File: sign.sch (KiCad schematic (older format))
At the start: 142 parts, among them J1 CONN_01X02, J2 CONN_01X02, J3 CONN_01X02, U1 APA102C_x6, U10 APA102C_x2, U100 APA102C_x6, U101 APA102C_x4, U102 APA102C_x2, U103 APA102C_x1, U104 APA102C_x3, U105 APA102C_x5, U106 APA102C_x2, U107 APA102C_x3, U108 APA102C_x10, U109 APA102C_x9, U11 APA102C_x2, U110 APA102C_x3, U111 APA102C_x12, U112 APA102C_x16, U113 APA102C_x8, U114 APA102C_x13, U115 APA102C_x3, U116 APA102C_x6, U117 APA102C_x3, U118 APA102C_x6, U119 APA102C_x3, U12 APA102C_x2, U120 APA102C_x2, U121 APA102C_x6, U122 APA102C_x3, U123 APA102C_x6, U124 APA102C_x7, U125 APA102C_x12, U126 APA102C_x6, U127 APA102C_x11, U128 APA102C_x4, U129 APA102C_x6, U13 APA102C_x2, U130 APA102C_x2, U131 APA102C_x2, U132 APA102C_x3, U133 APA102C_x1, U134 APA102C_x3, U135 APA102C_x3, U136 APA102C_x12, U137 APA102C_x12, U138 APA102C_x9, U139 APA102C_x4, U14 APA102C_x3, U15 APA102C_x3, U16 APA102C_x3, U17 APA102C_x3, U18 APA102C_x5, U19 APA102C_x6, U2 APA102C_x8, U20 APA102C_x2, U21 APA102C_x7, U22 APA102C_x5, U23 APA102C_x7, U24 APA102C_x3, U25 APA102C_x2, U26 APA102C_x7, U27 APA102C_x2, U28 APA102C_x3, U29 APA102C_x5, U3 APA102C_x11, U30 APA102C_x2, U31 APA102C_x5, U32 APA102C_x2, U33 APA102C_x8, U34 APA102C_x9, U35 APA102C_x3, U36 APA102C_x2, U37 APA102C_x5, U38 APA102C_x11, U39 APA102C_x6, U4 APA102C_x6, U40 APA102C_x4, U41 APA102C_x5, U42 APA102C_x3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

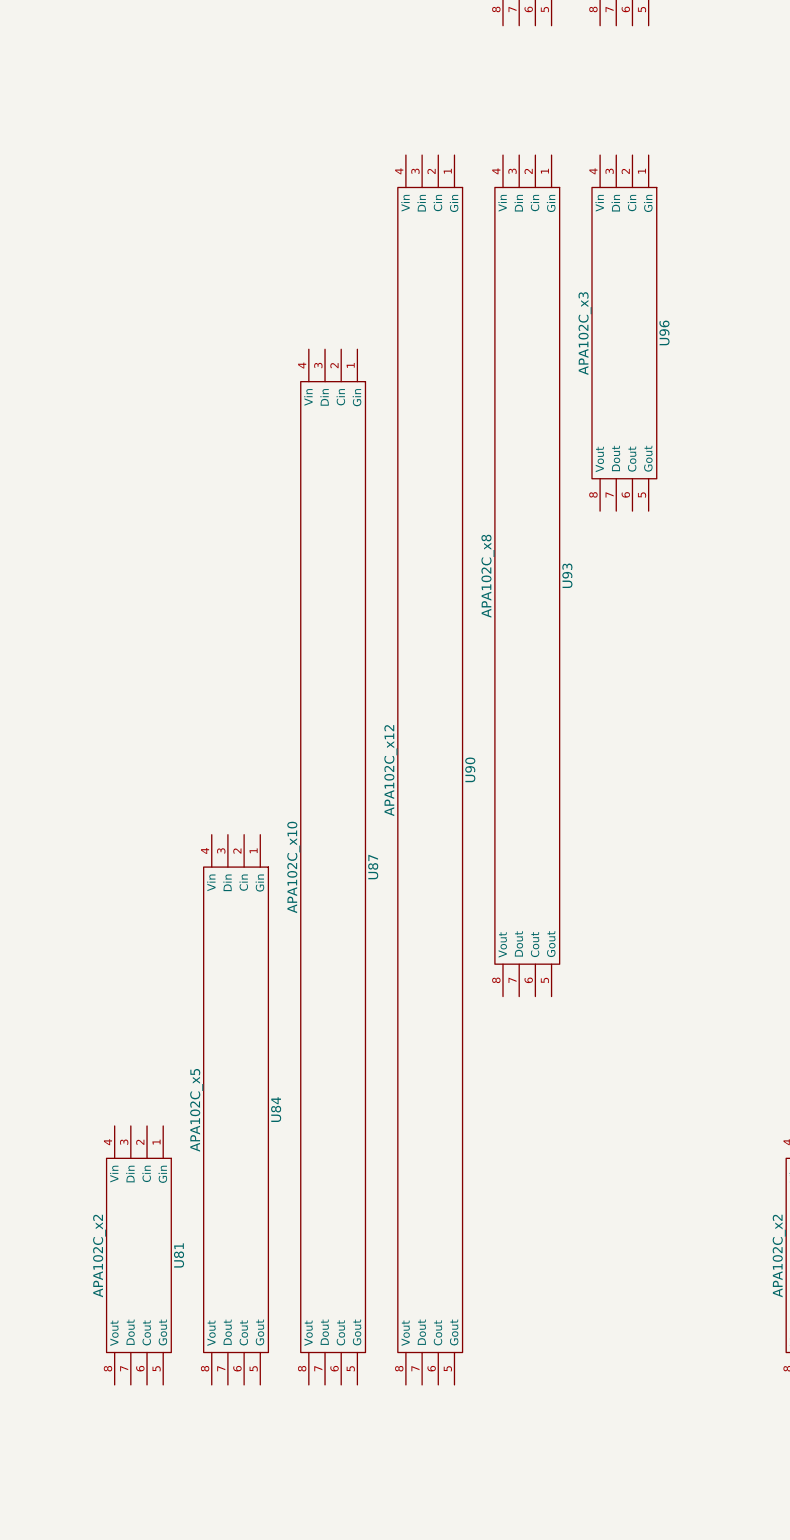
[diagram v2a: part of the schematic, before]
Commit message: nets for 'i'
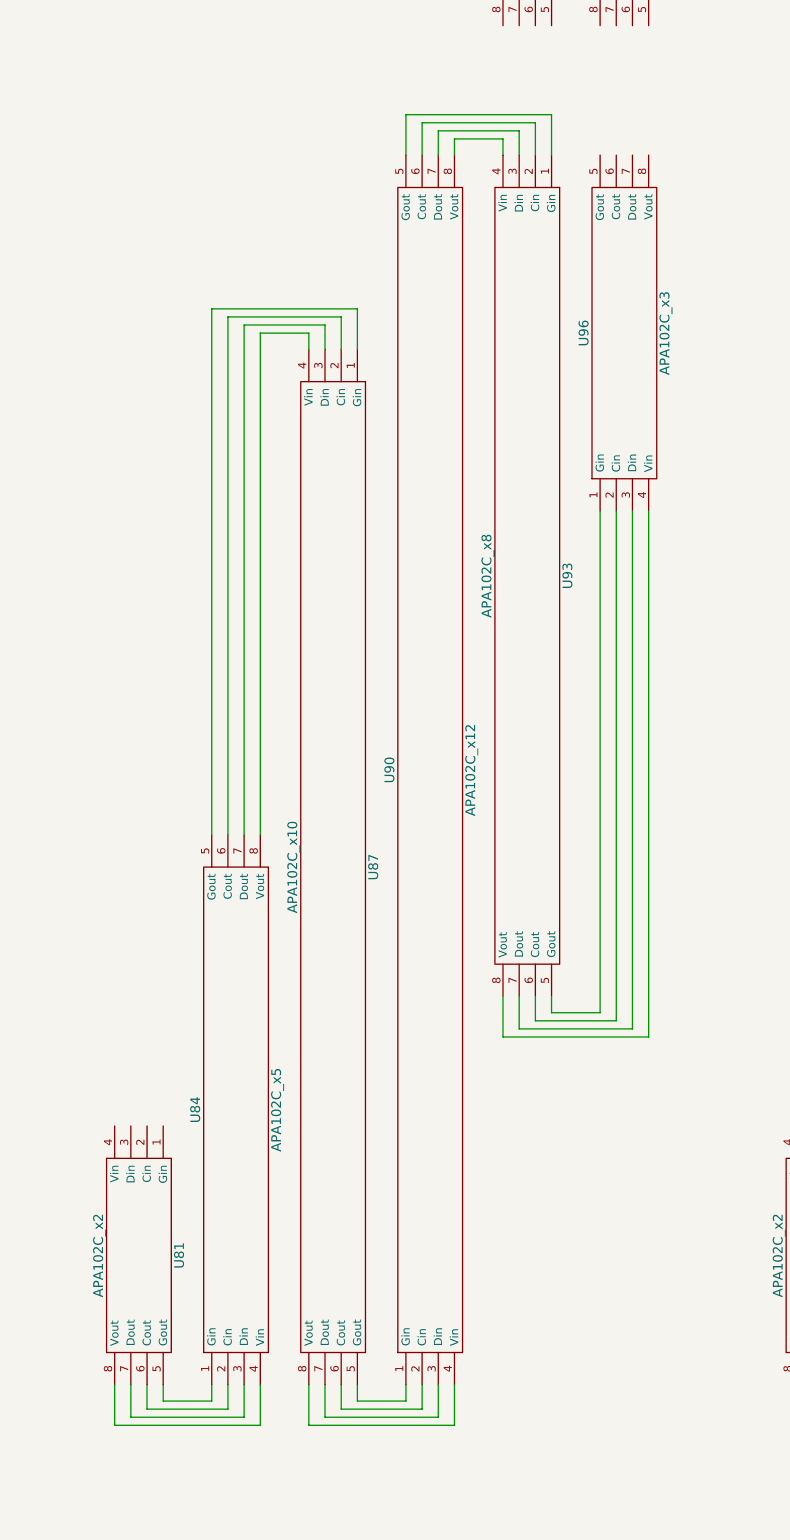
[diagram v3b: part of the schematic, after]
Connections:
- net at U81.5 (Gout): now also U84.1 (Gin)
- net at U81.6 (Cout): now also U84.2 (Cin)
- net at U81.7 (Dout): now also U84.3 (Din)
- net at U81.8 (Vout): now also U84.4 (Vin)
- net at U84.5 (Gout): now also U87.1 (Gin)
- net at U84.6 (Cout): now also U87.2 (Cin)
- net at U84.7 (Dout): now also U87.3 (Din)
- net at U84.8 (Vout): now also U87.4 (Vin)
- net at U87.5 (Gout): now also U90.1 (Gin)
- net at U87.6 (Cout): now also U90.2 (Cin)
- net at U87.7 (Dout): now also U90.3 (Din)
- net at U87.8 (Vout): now also U90.4 (Vin)
- net at U90.5 (Gout): now also U93.1 (Gin)
- net at U90.6 (Cout): now also U93.2 (Cin)
- net at U90.7 (Dout): now also U93.3 (Din)
- net at U90.8 (Vout): now also U93.4 (Vin)
- net at U93.5 (Gout): now also U96.1 (Gin)
- net at U93.6 (Cout): now also U96.2 (Cin)
- net at U93.7 (Dout): now also U96.3 (Din)
- net at U93.8 (Vout): now also U96.4 (Vin)
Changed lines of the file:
@@
 F 3 "" H 20100 24600 60  0001 C CNN
 	1    20100 24600
-	0    1    1    0
+	0    -1   -1   0
 $EndComp
 $Comp
@@
 F 3 "" H 21300 22500 60  0001 C CNN
 	1    21300 22500
-	0    1    1    0
+	0    -1   -1   0
 $EndComp
 $Comp
@@
 F 3 "" H 22500 19800 60  0001 C CNN
 	1    22500 19800
-	0    1    1    0
+	0    -1   -1   0
 $EndComp
 $Comp
@@
 	-1   0    0    1
 $EndComp
+Wire Wire Line
+	19650 26300 19650 26400
+Wire Wire Line
+	19650 26400 19950 26400
+Wire Wire Line
+	19950 26400 19950 26300
+Wire Wire Line
+	19550 26300 19550 26450
+Wire Wire Line
+	19550 26450 20050 26450
+Wire Wire Line
+	20050 26450 20050 26300
+Wire Wire Line
+	19450 26300 19450 26500
+Wire Wire Line
+	19450 26500 20150 26500
+Wire Wire Line
+	20150 26500 20150 26300
+Wire Wire Line
+	19350 26300 19350 26550
+Wire Wire Line
+	19350 26550 20250 26550
+Wire Wire Line
+	20250 26550 20250 26300
+Wire Wire Line
+	20850 26300 20850 26400
+Wire Wire Line
+	20850 26400 21150 26400
+Wire Wire Line
+	21150 26400 21150 26300
+Wire Wire Line
+	20750 26300 20750 26450
+Wire Wire Line
+	20750 26450 21250 26450
+Wire Wire Line
+	21250 26450 21250 26300
+Wire Wire Line
+	20650 26300 20650 26500
+Wire Wire Line
+	20650 26500 21350 26500
+Wire Wire Line
+	21350 26500 21350 26300
+Wire Wire Line
+	20550 26300 20550 26550
+Wire Wire Line
+	20550 26550 21450 26550
+Wire Wire Line
+	21450 26550 21450 26300
+Wire Wire Line
+	20250 22900 20250 19800
+Wire Wire Line
+	20250 19800 20550 19800
+Wire Wire Line
+	20550 19800 20550 19900
+Wire Wire Line
+	20650 19900 20650 19750
+Wire Wire Line
+	20650 19750 20150 19750
+Wire Wire Line
+	20150 19750 20150 22900
+Wire Wire Line
+	20050 22900 20050 19700
+Wire Wire Line
+	20050 19700 20750 19700
+Wire Wire Line
+	20750 19700 20750 19900
+Wire Wire Line
+	20850 19900 20850 19650
+Wire Wire Line
+	20850 19650 19950 19650
+Wire Wire Line
+	19950 19650 19950 22900
+Wire Wire Line
+	21450 18700 21450 18600
+Wire Wire Line
+	21450 18600 21750 18600
+Wire Wire Line
+	21750 18600 21750 18700
+Wire Wire Line
+	21350 18700 21350 18550
+Wire Wire Line
+	21350 18550 21850 18550
+Wire Wire Line
+	21850 18550 21850 18700
+Wire Wire Line
+	21950 18700 21950 18500
+Wire Wire Line
+	21950 18500 21250 18500
+Wire Wire Line
+	21250 18500 21250 18700
+Wire Wire Line
+	21150 18700 21150 18450
+Wire Wire Line
+	21150 18450 22050 18450
+Wire Wire Line
+	22050 18450 22050 18700
+Wire Wire Line
+	22050 23900 22050 24000
+Wire Wire Line
+	22050 24000 22350 24000
+Wire Wire Line
+	22350 24000 22350 20900
+Wire Wire Line
+	22450 20900 22450 24050
+Wire Wire Line
+	22450 24050 21950 24050
+Wire Wire Line
+	21950 24050 21950 23900
+Wire Wire Line
+	21850 24100 22550 24100
+Wire Wire Line
+	22550 24100 22550 20900
+Wire Wire Line
+	22650 20900 22650 24150
+Wire Wire Line
+	22650 24150 21750 24150
+Wire Wire Line
+	21750 24150 21750 23900
+Wire Wire Line
+	21850 23900 21850 24100
 $EndSCHEMATC

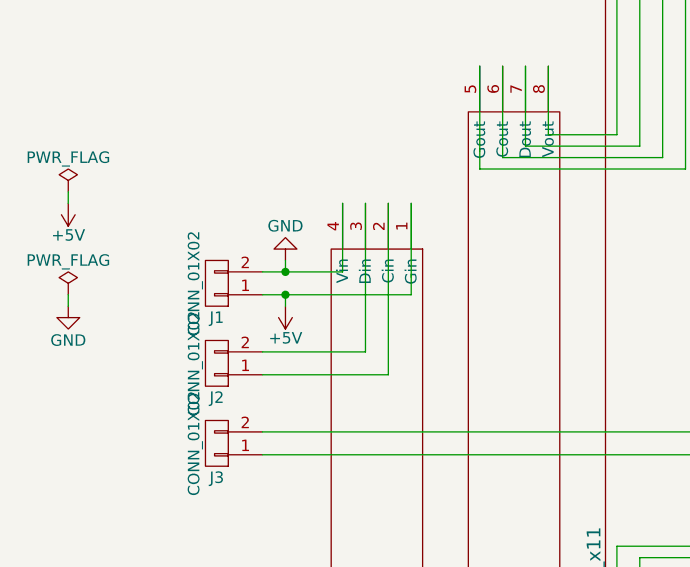
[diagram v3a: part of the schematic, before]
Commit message: Add cuts layer.
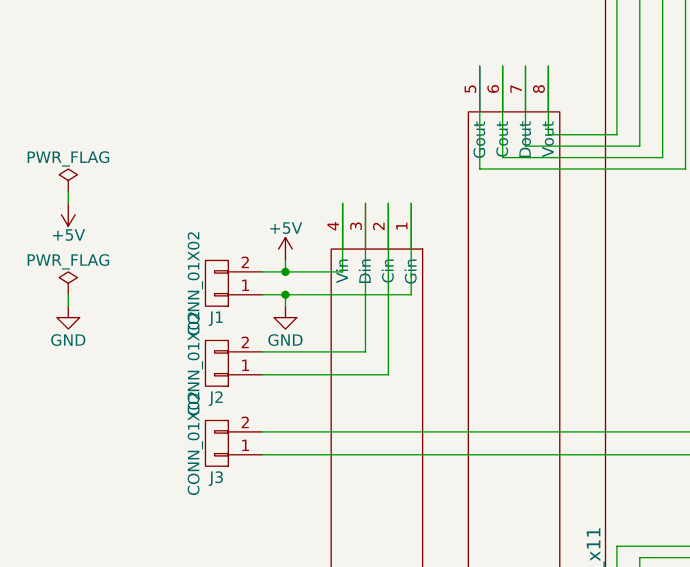
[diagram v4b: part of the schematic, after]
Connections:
- net +5V: now also J1.2 (P2), U1.4 (Vin); no longer J1.1 (P1), U1.1 (Gin)
- net GND: now also J1.1 (P1), U1.1 (Gin); no longer J1.2 (P2), U1.4 (Vin)
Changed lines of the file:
@@
 L +5V #PWR01
 U 1 1 5957C84C
-P 1700 7150
-F 0 "#PWR01" H 1700 7000 50  0001 C CNN
-F 1 "+5V" H 1700 7290 50  0000 C CNN
-F 2 "" H 1700 7150 50  0001 C CNN
-F 3 "" H 1700 7150 50  0001 C CNN
-	1    1700 7150
-	-1   0    0    1
+P 1700 6950
+F 0 "#PWR01" H 1700 6800 50  0001 C CNN
+F 1 "+5V" H 1700 7090 50  0000 C CNN
+F 2 "" H 1700 6950 50  0001 C CNN
+F 3 "" H 1700 6950 50  0001 C CNN
+	1    1700 6950
+	1    0    0    -1
 $EndComp
 $Comp
@@
 L GND #PWR06
 U 1 1 595636A7
-P 1700 6950
-F 0 "#PWR06" H 1700 6700 50  0001 C CNN
-F 1 "GND" H 1700 6800 50  0000 C CNN
-F 2 "" H 1700 6950 50  0001 C CNN
-F 3 "" H 1700 6950 50  0001 C CNN
-	1    1700 6950
-	-1   0    0    1
+P 1700 7150
+F 0 "#PWR06" H 1700 6900 50  0001 C CNN
+F 1 "GND" H 1700 7000 50  0000 C CNN
+F 2 "" H 1700 7150 50  0001 C CNN
+F 3 "" H 1700 7150 50  0001 C CNN
+	1    1700 7150
+	1    0    0    -1
 $EndComp
 Wire Wire Line

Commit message: Wire up some more letters.
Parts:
- added J4, J5, J6, J7, J8, J9: CONN_01X02, Pin_Headers:Pin_Header_Straight_1x02, symbol CONN_01X02
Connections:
- net +5V: now also U31.4 (Vin), U68.4 (Vin), J4.2 (P2), J7.2 (P2)
- net GND: now also U31.1 (Gin), U68.1 (Gin), J4.1 (P1), J7.1 (P1)
- net at U31.2 (Cin): now also J5.1 (P1)
- net at U31.3 (Din): now also J5.2 (P2)
- net at U31.5 (Gout): now also U34.1 (Gin)
- net at U31.6 (Cout): now also U34.2 (Cin)
- net at U31.7 (Dout): now also U34.3 (Din)
- net at U31.8 (Vout): now also U34.4 (Vin)
- net at U34.5 (Gout): now also U38.1 (Gin)
- net at U34.6 (Cout): now also U38.2 (Cin)
- net at U34.7 (Dout): now also U38.3 (Din)
- net at U34.8 (Vout): now also U38.4 (Vin)
- net at U38.5 (Gout): now also U42.1 (Gin)
- net at U38.6 (Cout): now also U42.2 (Cin)
- net at U38.7 (Dout): now also U42.3 (Din)
- net at U38.8 (Vout): now also U42.4 (Vin)
- net at U41.1 (Gin): now also U45.5 (Gout)
- net at U41.2 (Cin): now also U45.6 (Cout)
- net at U41.3 (Din): now also U45.7 (Dout)
- net at U41.4 (Vin): now also U45.8 (Vout)
- net at U41.6 (Cout): now also J6.1 (P1)
- net at U41.7 (Dout): now also J6.2 (P2)
- net at U42.5 (Gout): now also U46.1 (Gin)
- net at U42.6 (Cout): now also U46.2 (Cin)
- net at U42.7 (Dout): now also U46.3 (Din)
- net at U42.8 (Vout): now also U46.4 (Vin)
- net at U45.1 (Gin): now also U49.5 (Gout)
- net at U45.2 (Cin): now also U49.6 (Cout)
- net at U45.3 (Din): now also U49.7 (Dout)
- net at U45.4 (Vin): now also U49.8 (Vout)
- net at U46.5 (Gout): now also U50.1 (Gin)
- net at U46.6 (Cout): now also U50.2 (Cin)
- net at U46.7 (Dout): now also U50.3 (Din)
- net at U46.8 (Vout): now also U50.4 (Vin)
- net at U49.1 (Gin): now also U52.5 (Gout)
- net at U49.2 (Cin): now also U52.6 (Cout)
- net at U49.3 (Din): now also U52.7 (Dout)
- net at U49.4 (Vin): now also U52.8 (Vout)
- net at U50.5 (Gout): now also U53.1 (Gin)
- net at U50.6 (Cout): now also U53.2 (Cin)
- net at U50.7 (Dout): now also U53.3 (Din)
- net at U50.8 (Vout): now also U53.4 (Vin)
- net at U52.1 (Gin): now also U55.5 (Gout)
- net at U52.2 (Cin): now also U55.6 (Cout)
- net at U52.3 (Din): now also U55.7 (Dout)
- net at U52.4 (Vin): now also U55.8 (Vout)
- net at U53.5 (Gout): now also U56.1 (Gin)
- net at U53.6 (Cout): now also U56.2 (Cin)
- net at U53.7 (Dout): now also U56.3 (Din)
- net at U53.8 (Vout): now also U56.4 (Vin)
- net at U54.5 (Gout): now also U57.1 (Gin)
- net at U54.6 (Cout): now also U57.2 (Cin)
- net at U54.7 (Dout): now also U57.3 (Din)
- net at U54.8 (Vout): now also U57.4 (Vin)
- net at U55.1 (Gin): now also U66.5 (Gout)
- net at U55.2 (Cin): now also U66.6 (Cout)
- net at U55.3 (Din): now also U66.7 (Dout)
- net at U55.4 (Vin): now also U66.8 (Vout)
- net at U56.5 (Gout): now also U58.1 (Gin)
- net at U56.6 (Cout): now also U58.2 (Cin)
- net at U56.7 (Dout): now also U58.3 (Din)
- net at U56.8 (Vout): now also U58.4 (Vin)
- net at U57.5 (Gout): now also U59.1 (Gin)
- net at U57.6 (Cout): now also U59.2 (Cin)
- net at U57.7 (Dout): now also U59.3 (Din)
- net at U57.8 (Vout): now also U59.4 (Vin)
- net at U58.5 (Gout): now also U60.1 (Gin)
- net at U58.6 (Cout): now also U60.2 (Cin)
- net at U58.7 (Dout): now also U60.3 (Din)
- net at U58.8 (Vout): now also U60.4 (Vin)
- net at U59.5 (Gout): now also U61.1 (Gin)
- net at U59.6 (Cout): now also U61.2 (Cin)
- net at U59.7 (Dout): now also U61.3 (Din)
- net at U59.8 (Vout): now also U61.4 (Vin)
- net at U60.5 (Gout): now also U62.1 (Gin)
- net at U60.6 (Cout): now also U62.2 (Cin)
- net at U60.7 (Dout): now also U62.3 (Din)
- net at U60.8 (Vout): now also U62.4 (Vin)
- net at U61.5 (Gout): now also U63.1 (Gin)
- net at U61.6 (Cout): now also U63.2 (Cin)
- net at U61.7 (Dout): now also U63.3 (Din)
- net at U61.8 (Vout): now also U63.4 (Vin)
- net at U62.5 (Gout): now also U64.1 (Gin)
- net at U62.6 (Cout): now also U64.2 (Cin)
- net at U62.7 (Dout): now also U64.3 (Din)
- net at U62.8 (Vout): now also U64.4 (Vin)
- net at U63.5 (Gout): now also U65.1 (Gin)
- net at U63.6 (Cout): now also U65.2 (Cin)
- net at U63.7 (Dout): now also U65.3 (Din)
- net at U63.8 (Vout): now also U65.4 (Vin)
- net at U64.5 (Gout): now also U66.1 (Gin)
- net at U64.6 (Cout): now also U66.2 (Cin)
- net at U64.7 (Dout): now also U66.3 (Din)
- net at U64.8 (Vout): now also U66.4 (Vin)
- net at U65.5 (Gout): now also U67.1 (Gin)
- net at U65.6 (Cout): now also U67.2 (Cin)
- net at U65.7 (Dout): now also U67.3 (Din)
- net at U65.8 (Vout): now also U67.4 (Vin)
- net at U67.5 (Gout): now also U69.1 (Gin)
- net at U67.6 (Cout): now also U69.2 (Cin)
- net at U67.7 (Dout): now also U69.3 (Din)
- net at U67.8 (Vout): now also U69.4 (Vin)
- net at U68.2 (Cin): now also J8.1 (P1)
- net at U68.3 (Din): now also J8.2 (P2)
- net at U68.5 (Gout): now also U70.1 (Gin)
- net at U68.6 (Cout): now also U70.2 (Cin)
- net at U68.7 (Dout): now also U70.3 (Din)
- net at U68.8 (Vout): now also U70.4 (Vin)
- net at U69.5 (Gout): now also U72.1 (Gin)
- net at U69.6 (Cout): now also U72.2 (Cin)
- net at U69.7 (Dout): now also U72.3 (Din)
- net at U69.8 (Vout): now also U72.4 (Vin)
- net at U70.5 (Gout): now also U73.1 (Gin)
- net at U70.6 (Cout): now also U73.2 (Cin)
- net at U70.7 (Dout): now also U73.3 (Din)
- net at U70.8 (Vout): now also U73.4 (Vin)
- net at U71.5 (Gout): now also U74.1 (Gin)
- net at U71.6 (Cout): now also U74.2 (Cin)
- net at U71.7 (Dout): now also U74.3 (Din)
- net at U71.8 (Vout): now also U74.4 (Vin)
- net at U72.5 (Gout): now also U75.1 (Gin)
- net at U72.6 (Cout): now also U75.2 (Cin)
- net at U72.7 (Dout): now also U75.3 (Din)
- net at U72.8 (Vout): now also U75.4 (Vin)
- net at U73.5 (Gout): now also U77.1 (Gin)
- net at U73.6 (Cout): now also U77.2 (Cin)
- net at U73.7 (Dout): now also U77.3 (Din)
- net at U73.8 (Vout): now also U77.4 (Vin)
- net at U74.5 (Gout): now also U78.1 (Gin)
- net at U74.6 (Cout): now also U78.2 (Cin)
- net at U74.7 (Dout): now also U78.3 (Din)
- net at U74.8 (Vout): now also U78.4 (Vin)
- net at U76.1 (Gin): now also U79.5 (Gout)
- net at U76.2 (Cin): now also U79.6 (Cout)
- net at U76.3 (Din): now also U79.7 (Dout)
- net at U76.4 (Vin): now also U79.8 (Vout)
- net at U76.6 (Cout): now also J9.1 (P1)
- net at U76.7 (Dout): now also J9.2 (P2)
- net at U77.5 (Gout): now also U80.1 (Gin)
- net at U77.6 (Cout): now also U80.2 (Cin)
- net at U77.7 (Dout): now also U80.3 (Din)
- net at U77.8 (Vout): now also U80.4 (Vin)
- net at U79.1 (Gin): now also U82.5 (Gout)
- net at U79.2 (Cin): now also U82.6 (Cout)
- net at U79.3 (Din): now also U82.7 (Dout)
- net at U79.4 (Vin): now also U82.8 (Vout)
- net at U80.5 (Gout): now also U83.1 (Gin)
- net at U80.6 (Cout): now also U83.2 (Cin)
- net at U80.7 (Dout): now also U83.3 (Din)
- net at U80.8 (Vout): now also U83.4 (Vin)
- net at U82.1 (Gin): now also U85.5 (Gout)
- net at U82.2 (Cin): now also U85.6 (Cout)
- net at U82.3 (Din): now also U85.7 (Dout)
- net at U82.4 (Vin): now also U85.8 (Vout)
- net at U83.5 (Gout): now also U86.1 (Gin)
- net at U83.6 (Cout): now also U86.2 (Cin)
- net at U83.7 (Dout): now also U86.3 (Din)
- net at U83.8 (Vout): now also U86.4 (Vin)
- net at U85.1 (Gin): now also U88.5 (Gout)
- net at U85.2 (Cin): now also U88.6 (Cout)
- net at U85.3 (Din): now also U88.7 (Dout)
- net at U85.4 (Vin): now also U88.8 (Vout)
- net at U86.5 (Gout): now also U89.1 (Gin)
- net at U86.6 (Cout): now also U89.2 (Cin)
- net at U86.7 (Dout): now also U89.3 (Din)
- net at U86.8 (Vout): now also U89.4 (Vin)
- net at U88.1 (Gin): now also U103.5 (Gout)
- net at U88.2 (Cin): now also U103.6 (Cout)
- net at U88.3 (Din): now also U103.7 (Dout)
- net at U88.4 (Vin): now also U103.8 (Vout)
- net at U89.5 (Gout): now also U91.1 (Gin)
- net at U89.6 (Cout): now also U91.2 (Cin)
- net at U89.7 (Dout): now also U91.3 (Din)
- net at U89.8 (Vout): now also U91.4 (Vin)
- net at U91.5 (Gout): now also U94.1 (Gin)
- net at U91.6 (Cout): now also U94.2 (Cin)
- net at U91.7 (Dout): now also U94.3 (Din)
- net at U91.8 (Vout): now also U94.4 (Vin)
- net at U92.5 (Gout): now also U95.1 (Gin)
- net at U92.6 (Cout): now also U95.2 (Cin)
- net at U92.7 (Dout): now also U95.3 (Din)
- net at U92.8 (Vout): now also U95.4 (Vin)
- net at U94.5 (Gout): now also U97.1 (Gin)
- net at U94.6 (Cout): now also U97.2 (Cin)
- net at U94.7 (Dout): now also U97.3 (Din)
- net at U94.8 (Vout): now also U97.4 (Vin)
- net at U95.5 (Gout): now also U99.1 (Gin)
- net at U95.6 (Cout): now also U99.2 (Cin)
- net at U95.7 (Dout): now also U99.3 (Din)
- net at U95.8 (Vout): now also U99.4 (Vin)
- net at U97.5 (Gout): now also U100.1 (Gin)
- net at U97.6 (Cout): now also U100.2 (Cin)
- net at U97.7 (Dout): now also U100.3 (Din)
- net at U97.8 (Vout): now also U100.4 (Vin)
- net at U100.5 (Gout): now also U103.1 (Gin)
- net at U100.6 (Cout): now also U103.2 (Cin)
- net at U100.7 (Dout): now also U103.3 (Din)
- net at U100.8 (Vout): now also U103.4 (Vin)
